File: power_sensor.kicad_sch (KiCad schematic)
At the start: 2 parts, among them U3 INA234AxYBJ

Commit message: Added
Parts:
- R9: footprint (none) -> Resistor_THT:R_Axial_DIN0204_L3.6mm_D1.6mm_P5.08mm_Horizontal
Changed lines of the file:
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@@
 			)
 		)
-		(property "Footprint" ""
+		(property "Footprint" "Resistor_THT:R_Axial_DIN0204_L3.6mm_D1.6mm_P5.08mm_Horizontal"
 			(at 130.81 127.508 90)
 			(effects

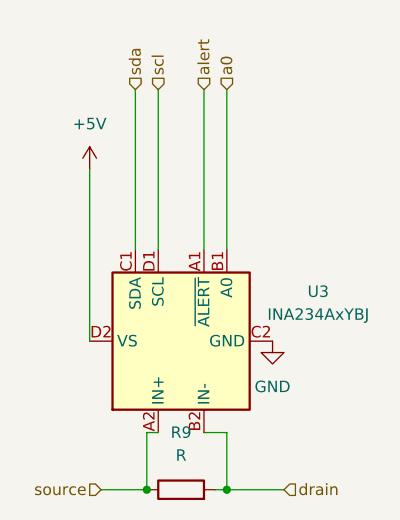
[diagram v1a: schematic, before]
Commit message: changed placement
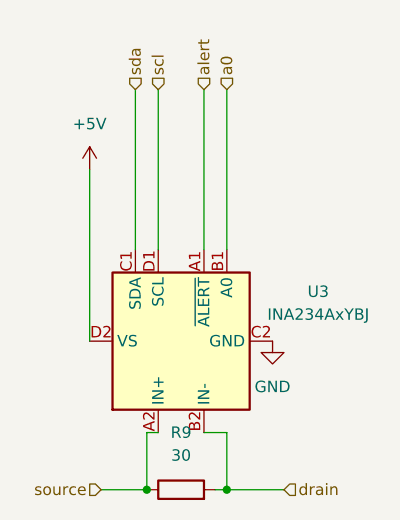
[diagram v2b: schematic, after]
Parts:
- R9: value R -> 30
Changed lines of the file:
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@@
 			)
 		)
-		(property "Value" "R"
+		(property "Value" "30"
 			(at 130.81 121.92 90)
 			(effects
